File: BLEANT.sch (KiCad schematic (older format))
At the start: 53 parts, among them IC1 FAN4010IL6X_F113, IC2 FAN4010IL6X_F113, J1 Conn_01x04_Male, J2 SC_19-20, J3 Conn_01x02, J4 Conn_01x02, J5 1909763-1, U1 nRF51x22-QFxx, U2 LM50BIM3, U3 MP5077GG-Z, U4 MP5077GG-Z, X2 32.768kHz, Y1 16MHz

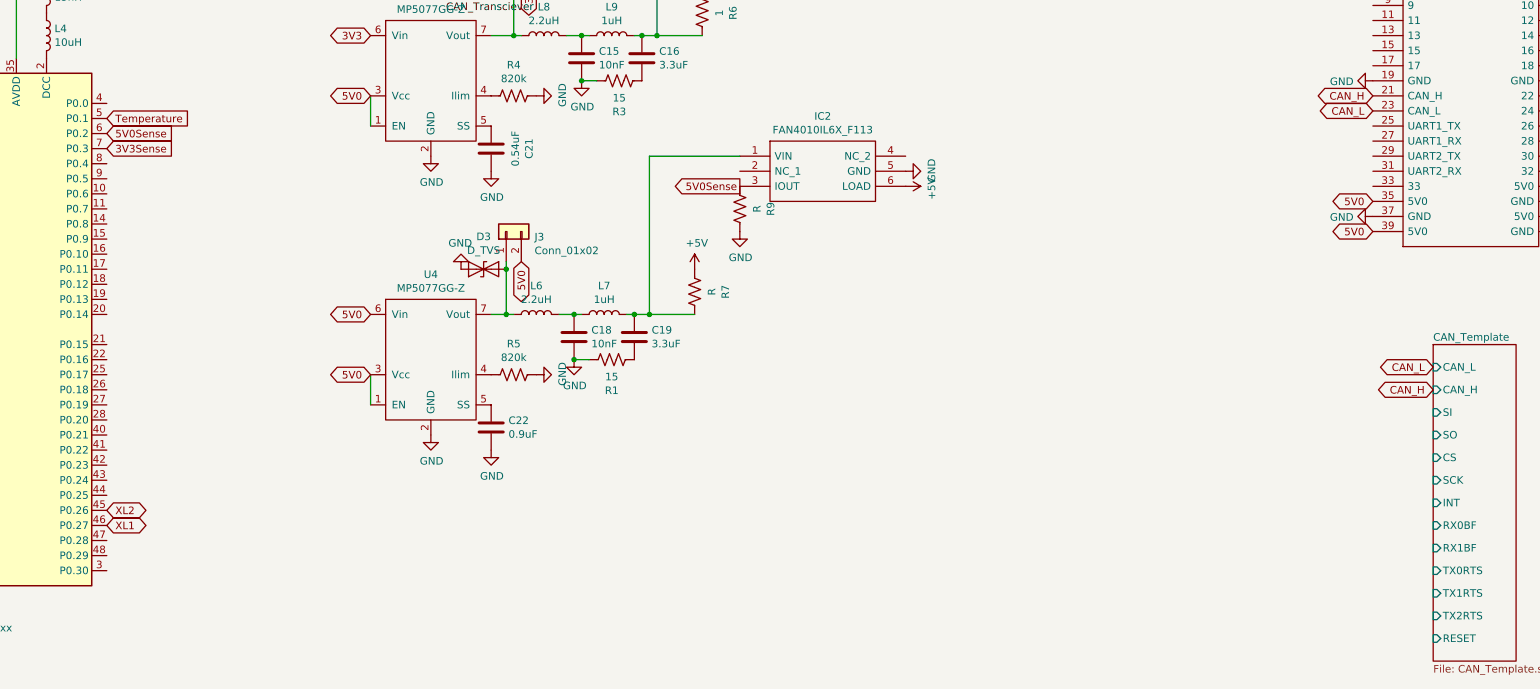
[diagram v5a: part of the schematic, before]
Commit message: Connected all IO lines
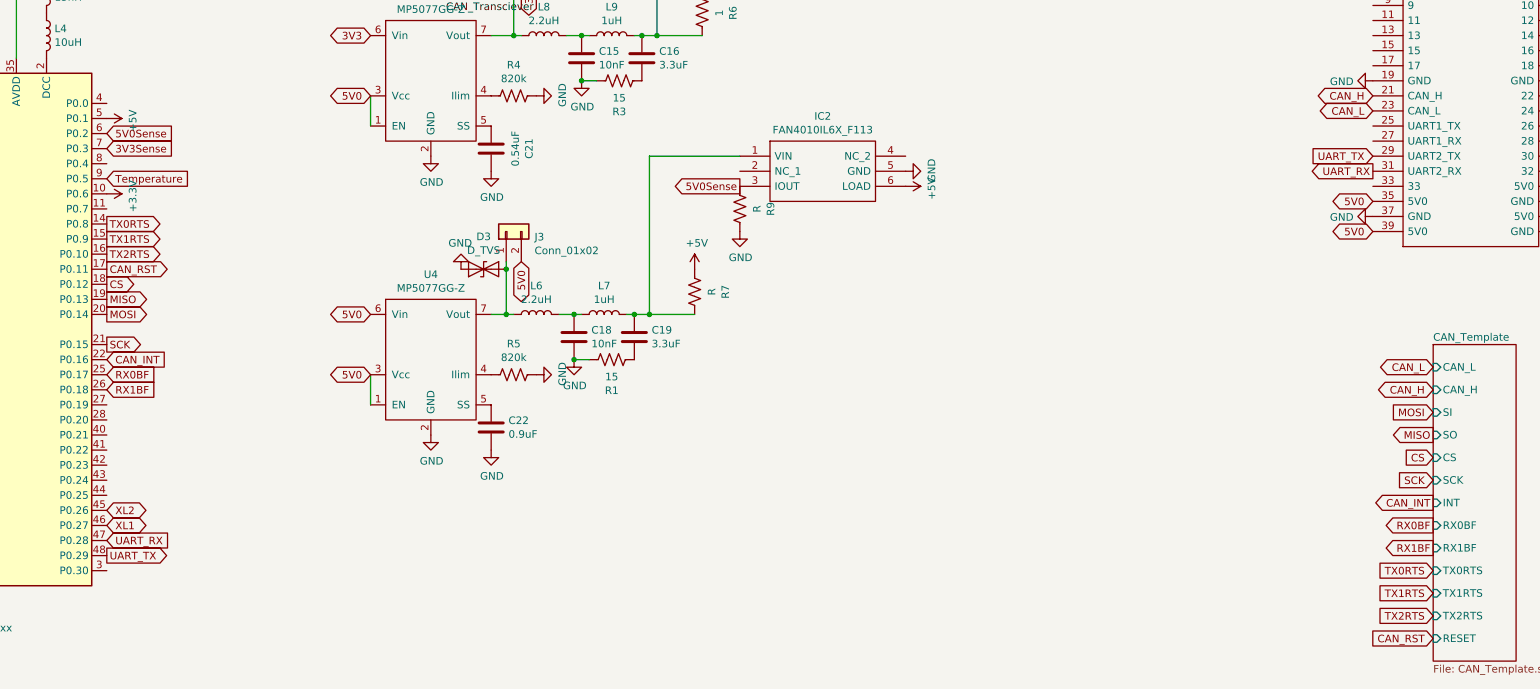
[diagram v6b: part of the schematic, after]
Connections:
- net +3V3: now also U1.10 (P0.6)
- net +5V: now also U1.5 (P0.1)
- net Temperature: now also U1.9 (P0.5); no longer U1.5 (P0.1)
- net TX0RTS: now reaches U1.14 (P0.8)
- net TX1RTS: now reaches U1.15 (P0.9)
- net TX2RTS: now reaches U1.16 (P0.10)
- net CAN_RST: now reaches U1.17 (P0.11)
- net CS: now reaches U1.18 (P0.12)
- net MISO: now reaches U1.19 (P0.13)
- net MOSI: now reaches U1.20 (P0.14)
- net SCK: now reaches U1.21 (P0.15)
- net CAN_INT: now reaches U1.22 (P0.16)
- net RX0BF: now reaches U1.25 (P0.17)
- net RX1BF: now reaches U1.26 (P0.18)
- net UART_RX: now reaches U1.47 (P0.28)
- net UART_RX: now also J2.31 (UART2_RX)
- net UART_TX: now reaches U1.48 (P0.29)
- net UART_TX: now also J2.29 (UART2_TX)
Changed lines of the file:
@@
 EESchema Schematic File Version 4
 LIBS:BLEANT-cache
-LIBS:CAN_Template-cache
 EELAYER 30 0
 EELAYER END
@@
 	-1   0    0    1
 $EndComp
-Text GLabel 4900 3000 2    50   Input ~ 0
+Text GLabel 4900 3400 2    50   Input ~ 0
 Temperature
 Text GLabel 4900 3100 2    50   Input ~ 0
@@
 Text GLabel 4900 3200 2    50   Input ~ 0
 3V3Sense
+$Comp
+L power:+3.3V #PWR0112
+U 1 1 5E3A3564
+P 4900 3500
+F 0 "#PWR0112" H 4900 3350 50  0001 C CNN
+F 1 "+3.3V" H 4915 3673 50  0000 C CNN
+F 2 "" H 4900 3500 50  0001 C CNN
+F 3 "" H 4900 3500 50  0001 C CNN
+	1    4900 3500
+	0    1    1    0
+$EndComp
+$Comp
+L power:+5V #PWR0113
+U 1 1 5E3A5E8B
+P 4900 3000
+F 0 "#PWR0113" H 4900 2850 50  0001 C CNN
+F 1 "+5V" H 4915 3173 50  0000 C CNN
+F 2 "" H 4900 3000 50  0001 C CNN
+F 3 "" H 4900 3000 50  0001 C CNN
+	1    4900 3000
+	0    1    1    0
+$EndComp
+Text GLabel 13700 4950 0    50   Input ~ 0
+MOSI
+Text GLabel 13700 5100 0    50   Output ~ 0
+MISO
+Text GLabel 13700 5250 0    50   Input ~ 0
+CS
+Text GLabel 13700 5400 0    50   Input ~ 0
+SCK
+Text GLabel 13700 6450 0    50   Input ~ 0
+CAN_RST
+Text GLabel 13700 5550 0    50   Output ~ 0
+CAN_INT
+Text GLabel 13700 5700 0    50   Output ~ 0
+RX0BF
+Text GLabel 13700 5850 0    50   Output ~ 0
+RX1BF
+Text GLabel 13700 6000 0    50   Input ~ 0
+TX0RTS
+Text GLabel 13700 6150 0    50   Input ~ 0
+TX1RTS
+Text GLabel 13700 6300 0    50   Input ~ 0
+TX2RTS
+Text GLabel 13300 3250 0    50   Input ~ 0
+UART_TX
+Text GLabel 13300 3350 0    50   Output ~ 0
+UART_RX
+Text GLabel 4900 5800 2    50   Input ~ 0
+UART_RX
+Text GLabel 4900 5900 2    50   Output ~ 0
+UART_TX
+Text GLabel 4900 3700 2    50   Output ~ 0
+TX0RTS
+Text GLabel 4900 3800 2    50   Output ~ 0
+TX1RTS
+Text GLabel 4900 3900 2    50   Output ~ 0
+TX2RTS
+Text GLabel 4900 4000 2    50   Output ~ 0
+CAN_RST
+Text GLabel 4900 4100 2    50   Output ~ 0
+CS
+Text GLabel 4900 4200 2    50   Output ~ 0
+MISO
+Text GLabel 4900 4300 2    50   Output ~ 0
+MOSI
+Text GLabel 4900 4500 2    50   Output ~ 0
+SCK
+Text GLabel 4900 4600 2    50   Input ~ 0
+CAN_INT
+Text GLabel 4900 4700 2    50   Input ~ 0
+RX0BF
+Text GLabel 4900 4800 2    50   Input ~ 0
+RX1BF
 $EndSCHEMATC
